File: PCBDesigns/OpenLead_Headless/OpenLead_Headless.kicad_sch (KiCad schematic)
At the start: 32 parts, among them J1 Conn_01x07_Pin, J2 Battery, J3 Conn_01x07_Pin, J4 Conn_01x01, J5 Conn_01x01, J6 Conn_01x01, Q8 AO3400A MOSFET, SW3 SW_SPDT, U10 LM4060 - 1.25V

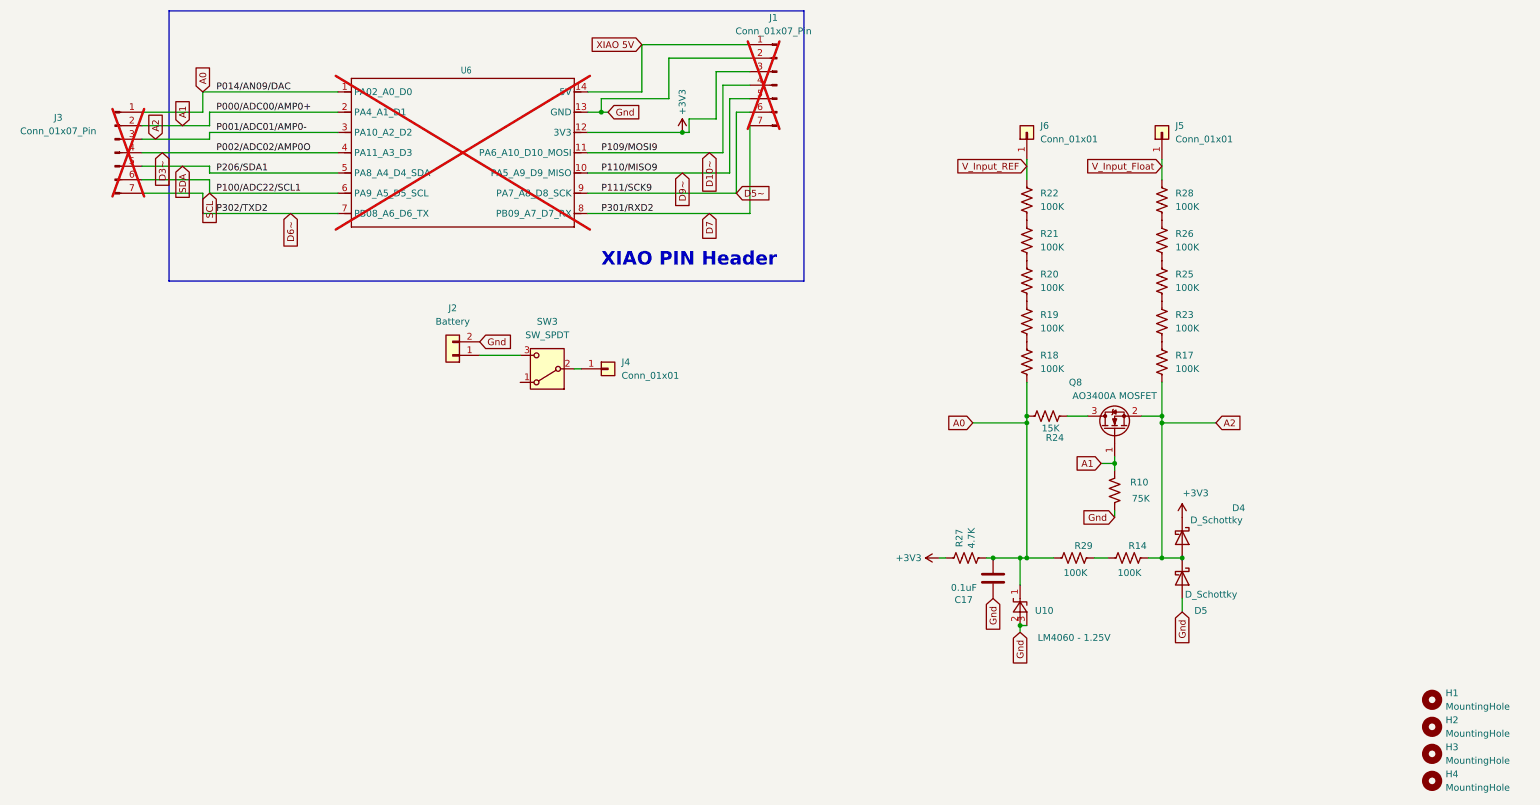
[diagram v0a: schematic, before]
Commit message: Housekeeping and some open-lead-detect diagnostic updates.
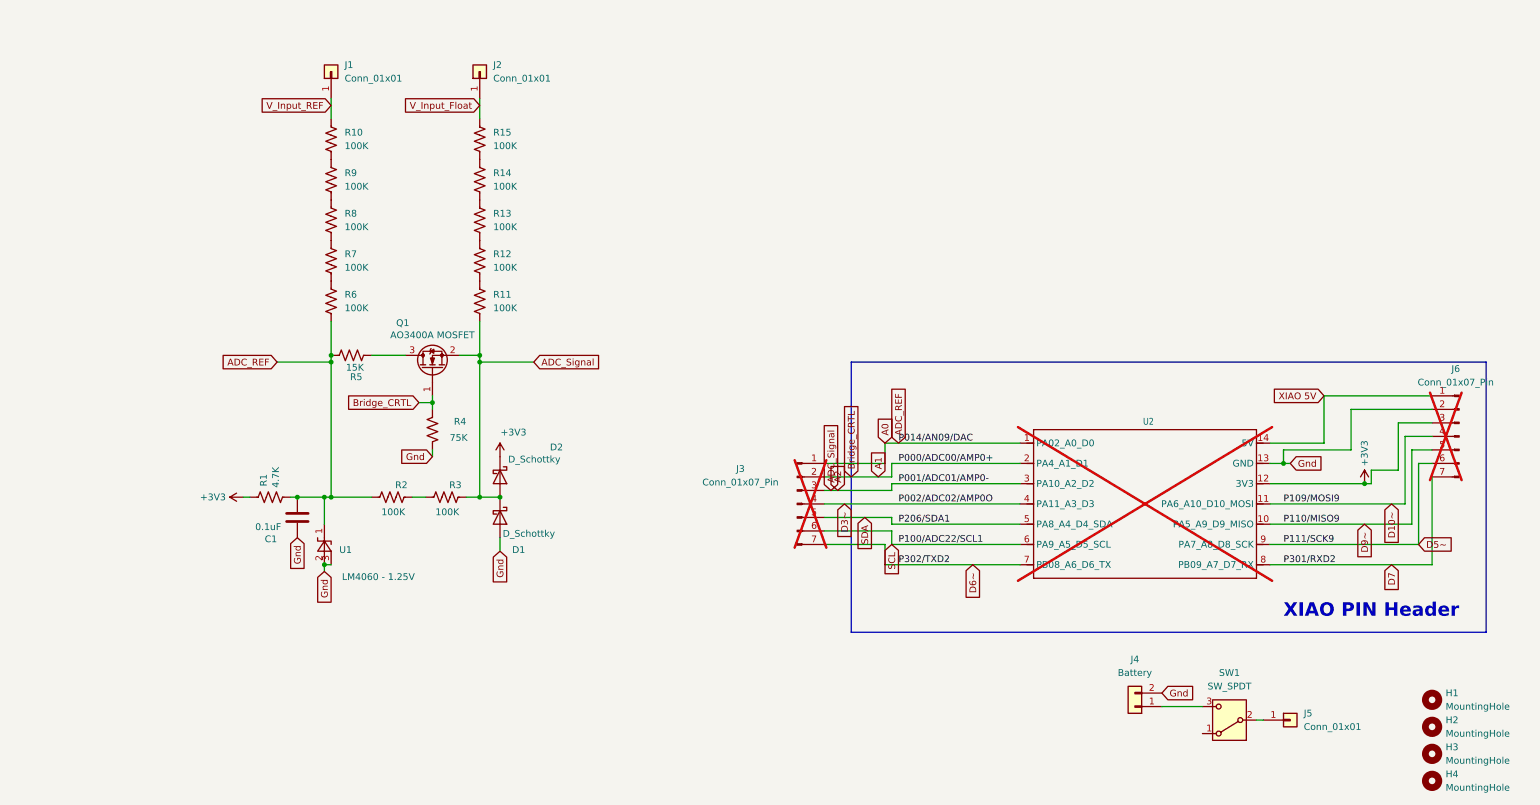
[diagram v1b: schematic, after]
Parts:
- renumbered C17 to C1, D5 to D1, D4 to D2, J6 to J1, J5 to J2, J2 to J4, J4 to J5, J1 to J6, Q8 to Q1, R27 to R1, R22 to R10, R17 to R11, R23 to R12, R25 to R13, R26 to R14, R28 to R15, R29 to R2, R14 to R3, R10 to R4, R24 to R5, R18 to R6, R19 to R7, R20 to R8, R21 to R9, SW3 to SW1, U10 to U1, U6 to U2
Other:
- moved on the sheet: C1, D1, D2, J1, J2, J3, J4, J5, J6, Q1, R1, R10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
